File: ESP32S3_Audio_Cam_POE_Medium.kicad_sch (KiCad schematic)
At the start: 241 parts, among them CN1 PJ-316C-6A, J1 Connector, USB-TYPE-C-16P, J10 Conn_01x02, J11 Conn_01x03, J12 Conn_01x02, J13 Conn_01x02, J14 Conn_01x03, J15 Conn_01x02, J16 Conn_01x02, J17 Conn_01x20_Pin, J18 Conn_01x20_Pin, J2 Conn_01x02, J3 Conn_01x02, J4 Conn_01x02, J5 Conn_01x02, J6 Conn_01x02, J7 Conn_01x03, J8 Conn_01x03, J9 Conn_01x02, Q1 AO3401A, Q2 AO3401A, Q3 AO3401A, Q4 AO3401A, Q5 AO3401A, Q6 AO3401A, Q7 AO3401A, U1 MT9221CT-06BR5, U10 ICS-43434, U11 ICS-43434, U3 USBLC6-2SC6, U4 ESP32-S3, U5 AXP2101, U6 DS18B20U(UMW), U7 W25Q128JVSIQ, U8 MAX98357AETE+T, U9 TM1637, Y1 40MHz, 15pF, Y2 32.768KHz

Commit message: Draft Medium
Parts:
- J10, J12, J13, J15, J16, J2, J3, J4, J5, J6, J9: footprint Connector_PinHeader_1.00mm:PinHeader_1x02_P1.00mm_Vertical -> Project-specific:PinHeader_1x02_P1.00mm_Vertical
- TP27, TP28, TP29, TP30, TP31, TP32, TP33, TP34, TP35, TP36, TP37, TP38, TP39, TP40, TP41, TP42, TP46: footprint Connector_PinHeader_1.00mm:PinHeader_1x01_P1.00mm_Vertical -> Project-specific:PinHeader_1x01_P1.00mm_Vertical

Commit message: Draft Medium
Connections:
- net 2U0RXD is gone; now on net U0RXD: J4.2 (Pin_2), U4.50 (U0RXD)
- net 2U0TXD is gone; now on net U0TXD: J4.1 (Pin_1), U4.49 (U0TXD)
- net +3V3: now also U1.1 (IP+), U1.2 (IP+); no longer J17.5 (Pin_5)
- net VBUS: no longer C1.1, U1.3 (IP-), U1.4 (IP-), U1.8 (VCC)
- net Vdrive: no longer U1.1 (IP+), U1.2 (IP+)
- new net VBUS+3V3: C1.1, J17.5 (Pin_5), U1.3 (IP-), U1.4 (IP-), U1.8 (VCC)
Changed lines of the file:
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@@
 	)
 	(junction
-		(at 33.02 -285.75)
-		(diameter 0)
-		(color 0 0 0 0)
-	)
-	(junction
 		(at 515.62 -116.84)
 		(diameter 0)
@@
 	(wire
 		(pts
-			(xy 33.02 -287.02) (xy 33.02 -285.75)
-		)
-		(stroke
-			(width 0)
-			(type default)
-		)
-	)
-	(wire
-		(pts
 			(xy 109.22 -127) (xy 123.19 -127)
 		)
@@
 		)
 	)
-	(label "2U0RXD"
+	(label "U0RXD"
 		(at 252.73 -146.05 0)
 		(effects
@@
 		)
 	)
-	(label "2U0TXD"
+	(label "U0TXD"
 		(at 252.73 -148.59 0)
 		(effects
@@
 			)
 		)
-		(property "Value" "Vdrive"
+		(property "Value" "+3V3"
 			(at 64.77 -285.7501 90)
 			(effects
@@
 	)
 	(symbol
+		(lib_id "power:+3V3")
+		(at 33.02 -285.75 90)
+		(unit 1)
+		(exclude_from_sim no)
+		(in_bom yes)
+		(on_board yes)
+		(dnp no)
+		(property "Reference" "#PWR06"
+			(at 36.83 -285.75 0)
+			(effects
+				(font
+					(size 1.27 1.27)
+				)
+				(hide yes)
+			)
+		)
+		(property "Value" "VBUS+3V3"
+			(at 25.4 -286.766 90)
+			(effects
+				(font
+					(size 1.27 1.27)
+				)
+			)
+		)
+		(property "Footprint" ""
+			(at 33.02 -285.75 0)
+			(effects
+				(font
+					(size 1.27 1.27)
+				)
+				(hide yes)
+			)
+		)
+		(property "Datasheet" ""
+			(at 33.02 -285.75 0)
+			(effects
+				(font
+					(size 1.27 1.27)
+				)
+				(hide yes)
+			)
+		)
+		(property "Description" "Power symbol creates a global label with name \"+3V3\""
+			(at 33.02 -285.75 0)
+			(effects
+				(font
+					(size 1.27 1.27)
+				)
+				(hide yes)
+			)
+		)
+		(pin "1"
+		)
+		(instances
+			(project "ESP32S3_Audio_Cam_POE_Medium"
+				(path "/c5870406-763b-471e-b639-251ff1f3739e"
+					(reference "#PWR06")
+					(unit 1)
+				)
+			)
+		)
+	)
+	(symbol
 		(lib_id "power:Earth")
 		(at 143.51 -113.03 0)
@@
 	)
 	(symbol
-		(lib_id "power:VBUS")
-		(at 33.02 -285.75 90)
-		(unit 1)
-		(exclude_from_sim no)
-		(in_bom yes)
-		(on_board yes)
-		(dnp no)
-		(fields_autoplaced yes)
-		(property "Reference" "#PWR02"
-			(at 36.83 -285.75 0)
-			(effects
-				(font
-					(size 1.27 1.27)
-				)
-				(hide yes)
-			)
-		)
-		(property "Value" "VBUS"
-			(at 29.21 -285.7501 90)
-			(effects
-				(font
-					(size 1.27 1.27)
-				)
-				(justify left)
-			)
-		)
-		(property "Footprint" ""
-			(at 33.02 -285.75 0)
-			(effects
-				(font
-					(size 1.27 1.27)
-				)
-				(hide yes)
-			)
-		)
-		(property "Datasheet" ""
-			(at 33.02 -285.75 0)
-			(effects
-				(font
-					(size 1.27 1.27)
-				)
-				(hide yes)
-			)
-		)
-		(property "Description" "Power symbol creates a global label with name \"VBUS\""
-			(at 33.02 -285.75 0)
-			(effects
-				(font
-					(size 1.27 1.27)
-				)
-				(hide yes)
-			)
-		)
-		(pin "1"
-		)
-		(instances
-			(project "ESP32S3_Audio_Cam_POE_Smaller"
-				(path "/c5870406-763b-471e-b639-251ff1f3739e"
-					(reference "#PWR02")
-					(unit 1)
-				)
-			)
-		)
-	)
-	(symbol
 		(lib_id "Connector:Conn_01x20_Pin")
 		(at 78.74 44.45 0)
@@
 		(on_board yes)
 		(dnp no)
-		(fields_autoplaced yes)
 		(property "Reference" "#PWR0112"
 			(at 69.85 31.75 0)
@@
 			)
 		)
-		(property "Value" "+3V3"
-			(at 62.23 31.7499 90)
+		(property "Value" "VBUS+3V3"
+			(at 58.42 30.734 90)
 			(effects
 				(font
 					(size 1.27 1.27)
 				)
-				(justify left)
 			)
 		)
@@
 			)
 		)
-		(property "Value" "VBUS"
+		(property "Value" "VBUS+3V3"
 			(at 64.77 -280.6701 90)
 			(effects

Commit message: Draft Medium
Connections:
- net 2GPIO39: now also J14.1 (Pin_1); no longer TP20.1
- net 2GPIO40: now also J11.1 (Pin_1); no longer TP21.1
- net 2GPIO41: now also J8.1 (Pin_1); no longer TP22.1
- net 2GPIO42: now also J7.1 (Pin_1); no longer TP23.1
- net 2GPIO45: now also R32.2; no longer TP24.1
- net RC.OTHR: no longer names the net of U4.18 (GPIO13)
- net RC.OTHR: now also TP24.1; no longer J14.1 (Pin_1)
- net RC.PAN: no longer names the net of U4.15 (GPIO10)
- net RC.PAN: now also TP21.1; no longer J7.1 (Pin_1)
- net RC.PWR: no longer names the net of U4.14 (GPIO9)
- net RC.PWR: now also TP20.1; no longer R32.2
- net RC.ROT: no longer names the net of U4.17 (GPIO12)
- net RC.ROT: now also TP23.1; no longer J11.1 (Pin_1)
- net RC.TILT: no longer names the net of U4.16 (GPIO11)
- net RC.TILT: now also TP22.1; no longer J8.1 (Pin_1)
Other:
- moved on the sheet: TP20, TP21, TP22, TP23, TP24

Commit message: DRAFT Medium
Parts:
- removed R12, R15: 100kΩ, PCM_JLCPCB:R_0402, symbol PCM_JLCPCB-Resistors:0402,100kΩ
- removed R14, R16: 10kΩ, PCM_JLCPCB:R_0402, symbol PCM_JLCPCB-Resistors:0402,10kΩ
- removed TP26: TestPoint, TestPoint:TestPoint_Pad_D1.0mm, symbol Connector:TestPoint
- added J19: Conn_01x03, Connector_PinHeader_2.54mm:PinHeader_1x03_P2.54mm_Vertical, symbol Connector_Generic:Conn_01x03
- added TST-R1: 0Ω, PCM_JLCPCB:R_0603, symbol PCM_JLCPCB-Resistors:0603,0Ω
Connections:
- net VBUS is gone; now on net Vdrive: D1.1, TST-R6.1
- net +3V3: no longer TST-R20.2, TST-R21.2, TST-R22.2, U1.1 (IP+), U1.2 (IP+)
- net 2USB_D+: no longer R13.2, U3.3 (I/O2)
- net 2USB_D-: no longer R11.2, U3.1 (I/O1)
- net COM: now also J19.3 (Pin_3)
- net ISEN.VO: now also U4.24 (GPIO18); no longer U4.23 (GPIO17)
- net PMU.Vo2: now also TST-R1.1
- net PMU.Vref: no longer TP5.1, U4.28 (SPICS1)
- net RC.VDD: now also J19.2 (Pin_2)
- net TEMP.DQ: now also U4.23 (GPIO17); no longer U4.24 (GPIO18)
- net Vdrive: now also U1.1 (IP+), U1.2 (IP+); no longer JP1.1 (A), R40.1, TST-R10.2, TST-R11.2, TST-R12.2, TST-R14.2, TST-R16.1, TST-R18.1, TST-R19.2, TST-R7.2, TST-R8.2
- net 2GPIO12: now reaches TP23.1, U4.17 (GPIO12)
- net 2GPIO11: now reaches TP22.1, U4.16 (GPIO11)
- net 2GPIO13: now reaches TP24.1, U4.18 (GPIO13)
- net 2GPIO9: now reaches TP20.1, U4.14 (GPIO9)
- net 2GPIO10: now reaches TP21.1, U4.15 (GPIO10)
- net 2GPIO39 renamed RC.OTHR
- net RC.OTHR: now also U4.51 (GPIO45); no longer U4.44 (MTCK)
- net 2GPIO40 renamed RC.PAN
- net RC.PAN: now also J7.1 (Pin_1); no longer J11.1 (Pin_1)
- net 2GPIO41 renamed RC.TILT
- net 2GPIO42 renamed RC.ROT
- net RC.ROT: now also J11.1 (Pin_1); no longer J7.1 (Pin_1)
- net 2GPIO45 renamed RC.PWR
- net RC.PWR: now also U4.44 (MTCK); no longer U4.51 (GPIO45)
- net 2GPIO46 renamed RC.OTHR2
- net RC.OTHR2: now also J19.1 (Pin_1)
- net VBus.Sense renamed 2GPIO14
- new net: R13.2, U3.3 (I/O2)
- new net: R11.2, U3.1 (I/O1)
- new net: TP5.1, U4.28 (SPICS1)
- new net Vdrive2: JP1.1 (A), R40.1, TST-R1.2, TST-R10.2, TST-R11.2, TST-R12.2, TST-R14.2, TST-R16.1, TST-R18.1, TST-R19.2, TST-R20.2, TST-R21.2, TST-R22.2, TST-R7.2, TST-R8.2
- no-connect marks 23 -> 45
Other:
- note added: "2GPIO39"
- note added: "2GPIO40"
- note added: "2GPIO41"
- note added: "2GPIO42"
- note added: "2GPIO45"
- note added: "2GPIO46"
- note removed: "2GPIO10"
- note removed: "2GPIO11"
- note removed: "2GPIO12"
- note removed: "2GPIO13"
- note removed: "2GPIO14"
- note removed: "2GPIO9"
- moved on the sheet: ANT1, BOOT1, BT1, C1, C10, C11, C12, C13, C14, C15, C16, C17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

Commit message: Draft Medium re-annotated.
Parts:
- renumbered C2 to C1, C19 to C10, C20 to C11, C9 to C12, C10 to C13, C59 to C14, C60 to C15, C54 to C16, C28 to C17, C30 to C18, C39 to C19, C23 to C2, C45 to C20, C55 to C21, C27 to C23, C33 to C24, C34 to C25, C35 to C26, C36 to C27, C41 to C28, C42 to C29, C1 to C3, C43 to C30, C47 to C31, C50 to C32, C51 to C33, C11 to C34, C12 to C35, C13 to C36, C14 to C37, C15 to C38, C61 to C39, C21 to C4, C62 to C40, C53 to C41, C56 to C42, C40 to C43, C26 to C44, C29 to C45, C31 to C46, C44 to C47, C52 to C48, C32 to C49, C24 to C5, C46 to C50, C48 to C51, C37 to C52, C38 to C53, C49 to C54, C17 to C55, C18 to C56, C16 to C57, C25 to C6, C57 to C7, C58 to C8, C8 to C9, D7 to D2, D9 to D3, D2 to D4, D8 to D6, D4 to D7, D3 to D8, D6 to D9, J5 to J10, J9 to J11, J7 to J12, J8 to J13, J11 to J14, J14 to J15, J19 to J16, J10 to J17, J6 to J18, J3 to J19, J17 to J2, J18 to J3, J16 to J4, J15 to J5, J4 to J6, J13 to J7, J12 to J8, J2 to J9, JP3 to JP2, JP4 to JP3, JP5 to JP4, JP6 to JP5, JP7 to JP6, JP2 to JP7, L4 to L1, L3 to L2, L5 to L3, L7 to L4, L6 to L5, L8 to L6, L9 to L7, PB2 to PB1, PB3 to PB2, PB4 to PB3, PB5 to PB4, PB1 to PB5, Q3 to Q2, Q6 to Q3, Q5 to Q4, Q2 to Q5, Q4 to Q6, R28 to R1, R6 to R10, R9 to R11, R42 to R12, R30 to R13, R39 to R14, R38 to R15, R17 to R16, R23 to R17, R33 to R18, R21 to R19, R8 to R2, R27 to R20, R36 to R21, R18 to R22, R24 to R23, R34 to R24, R31 to R25, R32 to R26, R7 to R27, R19 to R28, R25 to R29, R10 to R3, R35 to R30, R22 to R31, R29 to R32, R37 to R33, R26 to R34, R20 to R35, R11 to R4, R13 to R5, R40 to R6, R41 to R7, R43 to R8, R44 to R9, TP53 to TP1, TP11 to TP10, TP20 to TP11, TP21 to TP12, TP22 to TP13, TP23 to TP14, TP24 to TP15, TP18 to TP16, TP48 to TP17, TP50 to TP18, TP47 to TP19, TP55 to TP2, TP49 to TP20, TP27 to TP21, TP31 to TP22, TP35 to TP23, TP39 to TP24, TP46 to TP25, TP51 to TP26, TP28 to TP27, TP32 to TP28, TP36 to TP29, TP52 to TP3, TP40 to TP30, TP43 to TP31, TP29 to TP32, TP37 to TP34, TP41 to TP35, TP5 to TP36, TP10 to TP37, TP12 to TP38, TP13 to TP39, TP54 to TP4, TP14 to TP40, TP15 to TP41, TP16 to TP42, TP17 to TP43, TP19 to TP44, TP30 to TP45, TP34 to TP46, TP38 to TP47, TP42 to TP48, TP44 to TP49, TP4 to TP5, TP45 to TP50, TP25 to TP51, TST-R6 to TST-R1, TST-R24 to TST-R10, TST-R15 to TST-R11, TST-R13 to TST-R12, TST-R1 to TST-R13, TST-R7 to TST-R14, TST-R10 to TST-R15, TST-R14 to TST-R16, TST-R12 to TST-R18, TST-R9 to TST-R19, TST-R20 to TST-R2, TST-R8 to TST-R20, TST-R11 to TST-R21, TST-R16 to TST-R22, TST-R4 to TST-R3, TST-R18 to TST-R4, TST-R19 to TST-R5, TST-R21 to TST-R6, TST-R23 to TST-R7, TST-R5 to TST-R8, TST-R22 to TST-R9, U6 to U10, U3 to U2, U9 to U3, U8 to U4, U10 to U5, U11 to U6, U4 to U7, U5 to U8, U7 to U9

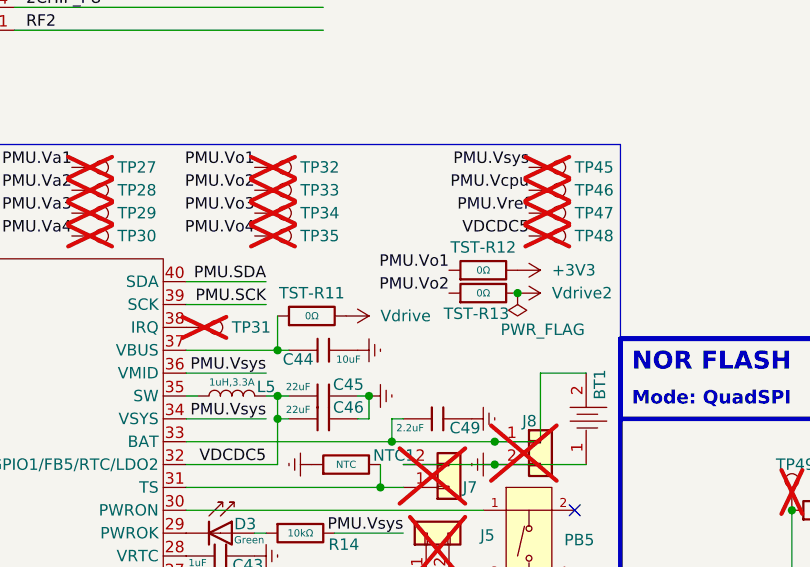
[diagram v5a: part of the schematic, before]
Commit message: Changed Vdrive2 net from PMU.Vo1 to VDCDC5
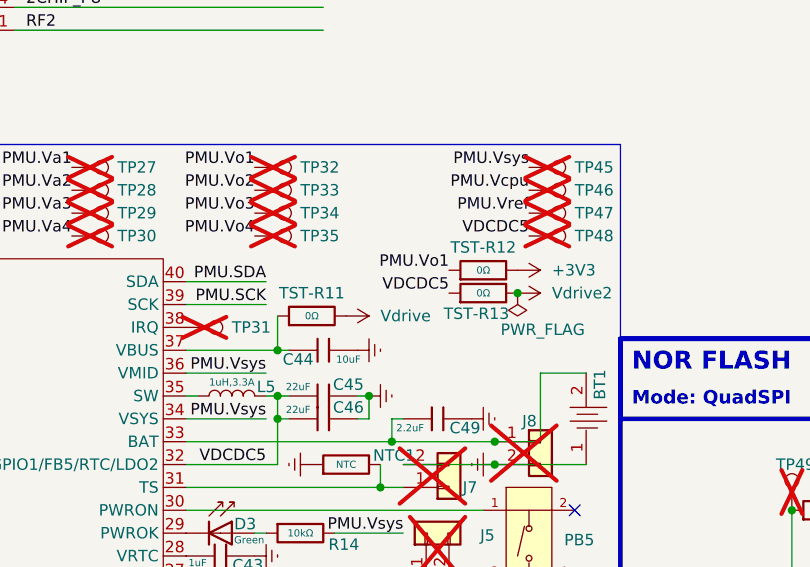
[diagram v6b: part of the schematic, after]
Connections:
- net PMU.Vo2: no longer TST-R13.1
- net VDCDC5: now also TST-R13.1
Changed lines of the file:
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@@
 		)
 	)
-	(label "PMU.Vo2"
+	(label "VDCDC5"
 		(at 303.53 119.38 180)
 		(effects

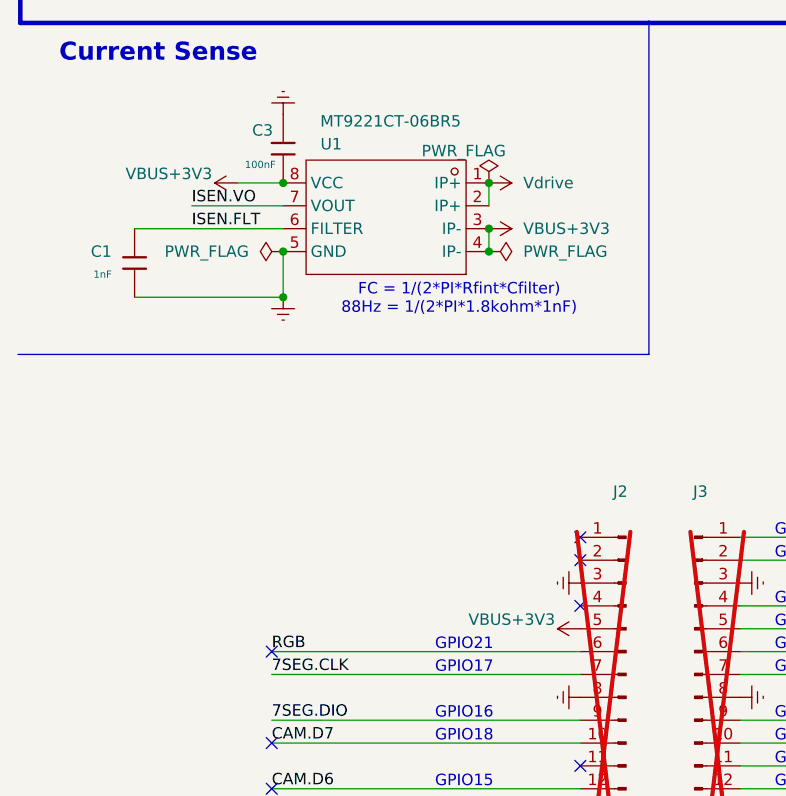
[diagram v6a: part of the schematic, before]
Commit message: Changed input power from 3.3V to 5V.
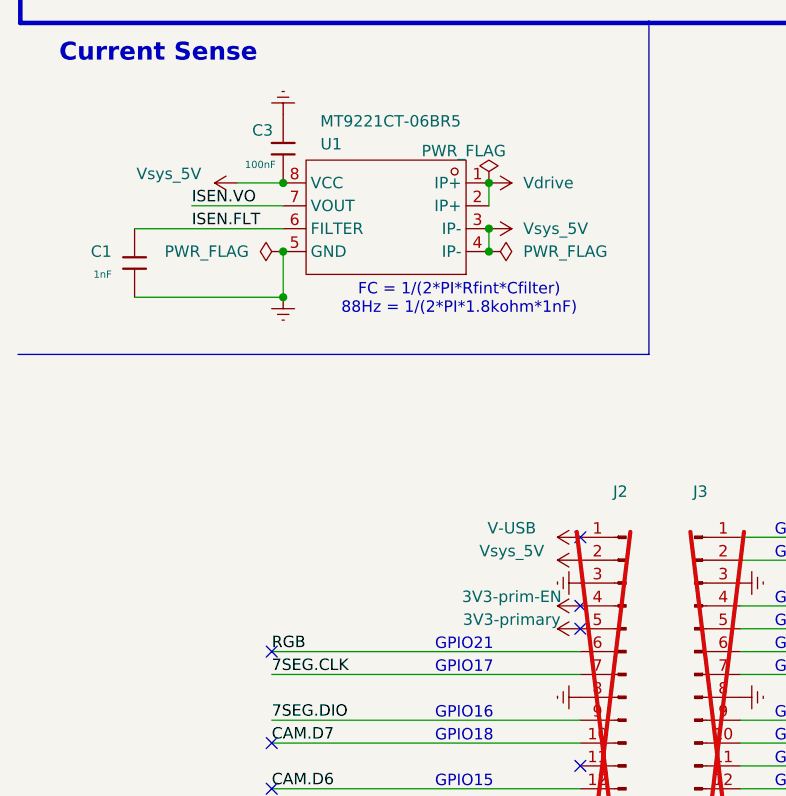
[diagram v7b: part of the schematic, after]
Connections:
- net V-USB: now reaches J2.1 (Pin_1)
- net Vsys_5V: now reaches J2.2 (Pin_2)
- net Vsys_5V: now also C3.1, U1.3 (IP-), U1.4 (IP-), U1.8 (VCC)
- net 3V3-prim-EN: now reaches J2.4 (Pin_4)
- removed net VBUS+3V3: C3.1, J2.5 (Pin_5), U1.3 (IP-), U1.4 (IP-), U1.8 (VCC)
- new net 3V3-primary: J2.5 (Pin_5)
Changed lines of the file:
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@@
 	)
 	(no_connect
-		(at 74.93 196.85)
+		(at 74.93 204.47)
 	)
 	(no_connect
@@
 			)
 		)
-		(property "Value" "VBUS+3V3"
+		(property "Value" "Vsys_5V"
 			(at 29.21 153.924 90)
 			(effects
@@
 			)
 		)
-		(property "Value" "VBUS+3V3"
+		(property "Value" "3V3-primary"
 			(at 67.31 203.454 90)
 			(effects
@@
 	)
 	(symbol
+		(lib_id "power:+3V3")
+		(at 74.93 196.85 90)
+		(unit 1)
+		(exclude_from_sim no)
+		(in_bom yes)
+		(on_board yes)
+		(dnp no)
+		(property "Reference" "#PWR0127"
+			(at 78.74 196.85 0)
+			(effects
+				(font
+					(size 1.27 1.27)
+				)
+				(hide yes)
+			)
+		)
+		(property "Value" "Vsys_5V"
+			(at 67.31 195.834 90)
+			(effects
+				(font
+					(size 1.27 1.27)
+				)
+			)
+		)
+		(property "Footprint" ""
+			(at 74.93 196.85 0)
+			(effects
+				(font
+					(size 1.27 1.27)
+				)
+				(hide yes)
+			)
+		)
+		(property "Datasheet" ""
+			(at 74.93 196.85 0)
+			(effects
+				(font
+					(size 1.27 1.27)
+				)
+				(hide yes)
+			)
+		)
+		(property "Description" "Power symbol creates a global label with name \"+3V3\""
+			(at 74.93 196.85 0)
+			(effects
+				(font
+					(size 1.27 1.27)
+				)
+				(hide yes)
+			)
+		)
+		(pin "1"
+		)
+		(instances
+			(project "ESP32S3_Audio_Cam_POE_Medium"
+				(path "/c5870406-763b-471e-b639-251ff1f3739e"
+					(reference "#PWR0127")
+					(unit 1)
+				)
+			)
+		)
+	)
+	(symbol
 		(lib_id "Connector:TestPoint")
 		(at 181.61 34.29 90)
@@
 	)
 	(symbol
+		(lib_id "power:+3V3")
+		(at 74.93 194.31 90)
+		(unit 1)
+		(exclude_from_sim no)
+		(in_bom yes)
+		(on_board yes)
+		(dnp no)
+		(property "Reference" "#PWR0128"
+			(at 78.74 194.31 0)
+			(effects
+				(font
+					(size 1.27 1.27)
+				)
+				(hide yes)
+			)
+		)
+		(property "Value" "V-USB"
+			(at 67.31 193.294 90)
+			(effects
+				(font
+					(size 1.27 1.27)
+				)
+			)
+		)
+		(property "Footprint" ""
+			(at 74.93 194.31 0)
+			(effects
+				(font
+					(size 1.27 1.27)
+				)
+				(hide yes)
+			)
+		)
+		(property "Datasheet" ""
+			(at 74.93 194.31 0)
+			(effects
+				(font
+					(size 1.27 1.27)
+				)
+				(hide yes)
+			)
+		)
+		(property "Description" "Power symbol creates a global label with name \"+3V3\""
+			(at 74.93 194.31 0)
+			(effects
+				(font
+					(size 1.27 1.27)
+				)
+				(hide yes)
+			)
+		)
+		(pin "1"
+		)
+		(instances
+			(project "ESP32S3_Audio_Cam_POE_Medium"
+				(path "/c5870406-763b-471e-b639-251ff1f3739e"
+					(reference "#PWR0128")
+					(unit 1)
+				)
+			)
+		)
+	)
+	(symbol
 		(lib_id "Connector_Generic:Conn_01x02")
 		(at 313.69 135.89 0)
@@
 			)
 		)
-		(property "Value" "VBUS+3V3"
+		(property "Value" "Vsys_5V"
 			(at 68.58 160.0199 90)
 			(effects
@@
 					(unit 1)
 				)
+			)
+		)
+	)
+	(symbol
+		(lib_id "power:+3V3")
+		(at 74.93 201.93 90)
+		(unit 1)
+		(exclude_from_sim no)
+		(in_bom yes)
+		(on_board yes)
+		(dnp no)
+		(property "Reference" "#PWR0129"
+			(at 78.74 201.93 0)
+			(effects
+				(font
+					(size 1.27 1.27)
+				)
+				(hide yes)
+			)
+		)
+		(property "Value" "3V3-prim-EN"
+			(at 67.31 200.914 90)
+			(effects
+				(font
+					(size 1.27 1.27)
+				)
+			)
+		)
+		(property "Footprint" ""
+			(at 74.93 201.93 0)
+			(effects
+				(font
+					(size 1.27 1.27)
+				)
+				(hide yes)
+			)
+		)
+		(property "Datasheet" ""
+			(at 74.93 201.93 0)
+			(effects
+				(font
+					(size 1.27 1.27)
+				)
+				(hide yes)
+			)
+		)
+		(property "Description" "Power symbol creates a global label with name \"+3V3\""
+			(at 74.93 201.93 0)
+			(effects
+				(font
+					(size 1.27 1.27)
+				)
+				(hide yes)
+			)
+		)
+		(pin "1"
+		)
+		(instances
+			(project "ESP32S3_Audio_Cam_POE_Medium"
+				(path "/c5870406-763b-471e-b639-251ff1f3739e"
+					(reference "#PWR0129")
+					(unit 1)
+				)
